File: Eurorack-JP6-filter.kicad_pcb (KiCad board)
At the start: 2 copper layers, 65 x 100 mm, 153 parts, among them J1 JACK_MONO_SW, J2 JACK_MONO_SW, J3 JACK_MONO_SW, J4 JACK_MONO_SW, J5 JACK_MONO_SW, J6 JACK_MONO_SW, P1 CONN_02X05, Q1 BCM857BS, Q2 BCM857BS, Q3 J112, Q4 J112, Q5 J112, Q6 J112, SW1 KS-01Q, U1 TL072-, U10 CD4027, U11 CD40106, U12 TS321, U13 TS321, U2 TL072-, U3 TL072-, U4 TL072-, U5 LM13700, U6 LM13700, U7 LM13700, U8 DG409, U9 CD4052

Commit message: cleaned up silkscreen a bit. ready to do panel alignment test
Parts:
- VR6: value 50K -> 50K A
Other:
- board text added: "CV 1 BI"
- board text added: "CV 2 UNI"
- board text added: "FREQ"
- board text added: "IN 1"
- board text added: "IN 2"
- board text added: "LEVEL 2"
- board text added: "M I M O I D"
- board text added: "MODE"
- board text added: "OUT"
- board text added: "RES"
- board text added: "RES CV"
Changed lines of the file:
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@@
     (area 11.949999 11.949999 77.050001 112.050001)
     (thickness 1.6)
-    (drawings 205)
-    (tracks 1138)
+    (drawings 216)
+    (tracks 1135)
     (zones 0)
     (modules 153)
@@
     (descr http://www.bourns.com/docs/Product-Datasheets/TC33.pdf)
     (tags "Bourns, trimmer")
-    (fp_text reference VR7 (at 0.85 -3.1) (layer B.SilkS)
+    (fp_text reference VR7 (at -2.85 1.6) (layer B.SilkS)
       (effects (font (size 0.8128 0.8128) (thickness 0.1524)) (justify mirror))
     )
@@
       (effects (font (thickness 0.3048)))
     )
-    (fp_text value 50K (at 0 9.99998 215) (layer F.SilkS)
+    (fp_text value "50K A" (at 0 9.99998 215) (layer F.SilkS)
       (effects (font (thickness 0.3048)))
     )
@@
   (module MyModules:PJ-301B-JACK-SLOTS (layer F.Cu)
     (at 19 106.5)
-    (fp_text reference J1 (at 4 -7) (layer F.SilkS)
+    (fp_text reference J1 (at 3.75 -4.75) (layer F.SilkS)
       (effects (font (size 1.5 1.5) (thickness 0.15)))
     )
@@
   (module MyModules:PJ-301B-JACK-SLOTS (layer F.Cu)
     (at 19 92.5)
-    (fp_text reference J2 (at 3.75 -7) (layer F.SilkS)
+    (fp_text reference J2 (at 3.5 -4.75) (layer F.SilkS)
       (effects (font (size 1.5 1.5) (thickness 0.15)))
     )
@@
   (module MyModules:PJ-301B-JACK-SLOTS (layer F.Cu)
     (at 70 92.5)
-    (fp_text reference J3 (at 4 -7) (layer F.SilkS)
+    (fp_text reference J3 (at 3.5 -4.75) (layer F.SilkS)
       (effects (font (size 1.5 1.5) (thickness 0.15)))
     )
@@
   (module MyModules:PJ-301B-JACK-SLOTS (layer F.Cu)
     (at 56 106.5)
-    (fp_text reference J4 (at 3.75 -7) (layer F.SilkS)
+    (fp_text reference J4 (at 3.5 -4.75) (layer F.SilkS)
       (effects (font (size 1.5 1.5) (thickness 0.15)))
     )
@@
   (module MyModules:PJ-301B-JACK-SLOTS (layer F.Cu)
     (at 33 106.5)
-    (fp_text reference J5 (at 4 -7) (layer F.SilkS)
+    (fp_text reference J5 (at 3.75 -4.75) (layer F.SilkS)
       (effects (font (size 1.5 1.5) (thickness 0.15)))
     )
@@
   (module MyModules:PJ-301B-JACK-SLOTS (layer F.Cu)
     (at 70 106.5)
-    (fp_text reference J6 (at 4 -7) (layer F.SilkS)
+    (fp_text reference J6 (at 3.5 -4.75) (layer F.SilkS)
       (effects (font (size 1.5 1.5) (thickness 0.15)))
     )
@@
     (at 33 81.5)
     (attr smd)
-    (fp_text reference R49 (at -2 0 90) (layer B.SilkS)
+    (fp_text reference R49 (at 0 -1.4 180) (layer B.SilkS)
       (effects (font (size 0.6096 0.6096) (thickness 0.1524)) (justify mirror))
     )
@@
       (xy 0.555814 2.531069)) (layer B.SilkS) (width 0.01))
   )
+  (gr_text MODE (at 54.75 15) (layer F.SilkS)
+    (effects (font (size 1.5 1.5) (thickness 0.3)))
+  )
+  (gr_text FREQ (at 37.25 15) (layer F.SilkS)
+    (effects (font (size 1.5 1.5) (thickness 0.3)))
+  )
+  (gr_text RES (at 30.75 56.5) (layer F.SilkS)
+    (effects (font (size 1.5 1.5) (thickness 0.3)))
+  )
+  (gr_text "LEVEL 2" (at 58.25 56.75) (layer F.SilkS)
+    (effects (font (size 1.5 1.5) (thickness 0.3)))
+  )
+  (gr_text OUT (at 70 99.25) (layer F.SilkS)
+    (effects (font (size 1.5 1.5) (thickness 0.3)))
+  )
+  (gr_text "IN 2" (at 56.25 99.25) (layer F.SilkS)
+    (effects (font (size 1.5 1.5) (thickness 0.3)))
+  )
+  (gr_text "IN 1" (at 33 99.5) (layer F.SilkS)
+    (effects (font (size 1.5 1.5) (thickness 0.3)))
+  )
+  (gr_text "RES CV" (at 19 99.25) (layer F.SilkS)
+    (effects (font (size 1.5 1.5) (thickness 0.3)))
+  )
+  (gr_text "CV 1\nBI" (at 23 84) (layer F.SilkS)
+    (effects (font (size 1.5 1.5) (thickness 0.3)))
+  )
+  (gr_text "CV 2\nUNI" (at 66.5 84) (layer F.SilkS)
+    (effects (font (size 1.5 1.5) (thickness 0.3)))
+  )
+  (gr_text "M I M O I D" (at 44.7 51.1) (layer F.SilkS)
+    (effects (font (size 1.5 1.5) (thickness 0.3)))
+  )
   (gr_line (start 65.343549 67.620649) (end 65.343549 67.620649) (layer B.SilkS) (width 0.35))
   (gr_line (start 65.343549 67.620649) (end 65.343549 67.620649) (layer B.SilkS) (width 0.35))
@@
     (effects (font (size 1.5 1.5) (thickness 0.3)) (justify mirror))
   )
-  (gr_text "Multimode Filter\nv1.3 10 2016\n" (at 67 83.25) (layer B.SilkS)
+  (gr_text "Multimode Filter\nv1.3 10 2016\n" (at 22.1 82.7) (layer B.SilkS)
     (effects (font (size 1.5 1.5) (thickness 0.3)) (justify mirror))
   )
-  (gr_text -12V (at 74.6 41.4) (layer B.SilkS)
+  (gr_text -12V (at 69.7 42.9 270) (layer B.SilkS)
     (effects (font (size 1.016 1.016) (thickness 0.254)) (justify mirror))
   )
-  (gr_text "RES\nADJ" (at 27.2 42.2) (layer B.SilkS)
+  (gr_text "RES\nADJ" (at 18.7 42) (layer B.SilkS)
     (effects (font (size 0.8128 0.8128) (thickness 0.1524)) (justify mirror))
   )
@@
   (segment (start 50.6491 79.5) (end 50.6491 82) (width 0.254) (layer B.Cu) (net 19))
   (segment (start 49.6 82) (end 50.6491 82) (width 0.254) (layer B.Cu) (net 19))
+  (segment (start 47.4 83.4) (end 57.3 83.4) (width 0.3556) (layer F.Cu) (net 20))
+  (segment (start 57.3 83.4) (end 59.3 81.4) (width 0.3556) (layer F.Cu) (net 20))
+  (segment (start 59.3 81.4) (end 59.3 77.1) (width 0.3556) (layer F.Cu) (net 20))
+  (segment (start 59.3 77.1) (end 58.131801 75.931801) (width 0.3556) (layer F.Cu) (net 20))
+  (segment (start 48.815759 43.035141) (end 46.057295 43.035141) (width 0.3556) (layer F.Cu) (net 20))
+  (segment (start 58.131801 75.931801) (end 58.131801 46.131801) (width 0.3556) (layer F.Cu) (net 20))
+  (segment (start 58.131801 46.131801) (end 55.035141 43.035141) (width 0.3556) (layer F.Cu) (net 20))
+  (segment (start 55.035141 43.035141) (end 48.815759 43.035141) (width 0.3556) (layer F.Cu) (net 20))
   (segment (start 40.899096 30.8991) (end 40.999996 31) (width 0.6096) (layer B.Cu) (net 20))
   (segment (start 39.25 30.8991) (end 40.899096 30.8991) (width 0.6096) (layer B.Cu) (net 20))
@@
   (segment (start 29.775685 36.474315) (end 21.918537 36.474315) (width 0.6096) (layer B.Cu) (net 20))
   (segment (start 35.3509 30.8991) (end 29.775685 36.474315) (width 0.6096) (layer B.Cu) (net 20))
-  (segment (start 54.8509 42.8509) (end 53.070597 42.8509) (width 0.3556) (layer F.Cu) (net 20))
-  (segment (start 58.131801 46.131801) (end 54.8509 42.8509) (width 0.3556) (layer F.Cu) (net 20))
   (segment (start 46.057295 43.035141) (end 46.057295 44.307295) (width 0.3556) (layer F.Cu) (net 20))
   (segment (start 46.057295 44.307295) (end 46.75 45) (width 0.3556) (layer F.Cu) (net 20))
@@
   (via (at 62.7 35.6) (size 1.27) (layers F.Cu B.Cu) (net 20))
   (via (at 46.057295 43.035141) (size 1.27) (drill 0.635) (layers F.Cu B.Cu) (net 20))
-  (segment (start 53.070597 42.8509) (end 49 42.8509) (width 0.3556) (layer F.Cu) (net 20))
-  (segment (start 48.815759 43.035141) (end 49 42.8509) (width 0.3556) (layer F.Cu) (net 20))
-  (segment (start 46.057295 43.035141) (end 48.815759 43.035141) (width 0.3556) (layer F.Cu) (net 20))
-  (segment (start 53.070597 42.8509) (end 53.099981 42.880284) (width 0.3556) (layer F.Cu) (net 20))
   (segment (start 45.162519 66.745691) (end 45.797518 66.110692) (width 0.3556) (layer F.Cu) (net 20))
   (segment (start 23.75 15) (end 27.8 15) (width 0.6096) (layer F.Cu) (net 20))
@@
   (segment (start 41.3 15) (end 46.601981 15) (width 0.6096) (layer F.Cu) (net 20))
   (segment (start 46.601981 15) (end 47.351981 14.25) (width 0.6096) (layer F.Cu) (net 20))
-  (segment (start 47.4 83.4) (end 57.3 83.4) (width 0.3556) (layer F.Cu) (net 20))
-  (segment (start 57.3 83.4) (end 59.3 81.4) (width 0.3556) (layer F.Cu) (net 20))
-  (segment (start 59.3 81.4) (end 59.3 77.1) (width 0.3556) (layer F.Cu) (net 20))
-  (segment (start 59.3 77.1) (end 58.131801 75.931801) (width 0.3556) (layer F.Cu) (net 20))
-  (segment (start 58.131801 75.931801) (end 58.131801 46.131801) (width 0.3556) (layer F.Cu) (net 20))
   (segment (start 40.255941 77.7) (end 40 77.7) (width 0.3556) (layer F.Cu) (net 20))
   (segment (start 36 81.7) (end 36 94.601975) (width 0.3556) (layer F.Cu) (net 20))

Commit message: Gerbers generated and checked
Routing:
- net GND: track 31.7 -> 34.5 mm, vias 15 -> 17
- net Net-(R2-Pad2): track 21.6 -> 20.6 mm
- net Net-(C3-Pad1): track 61.6 -> 62.3 mm

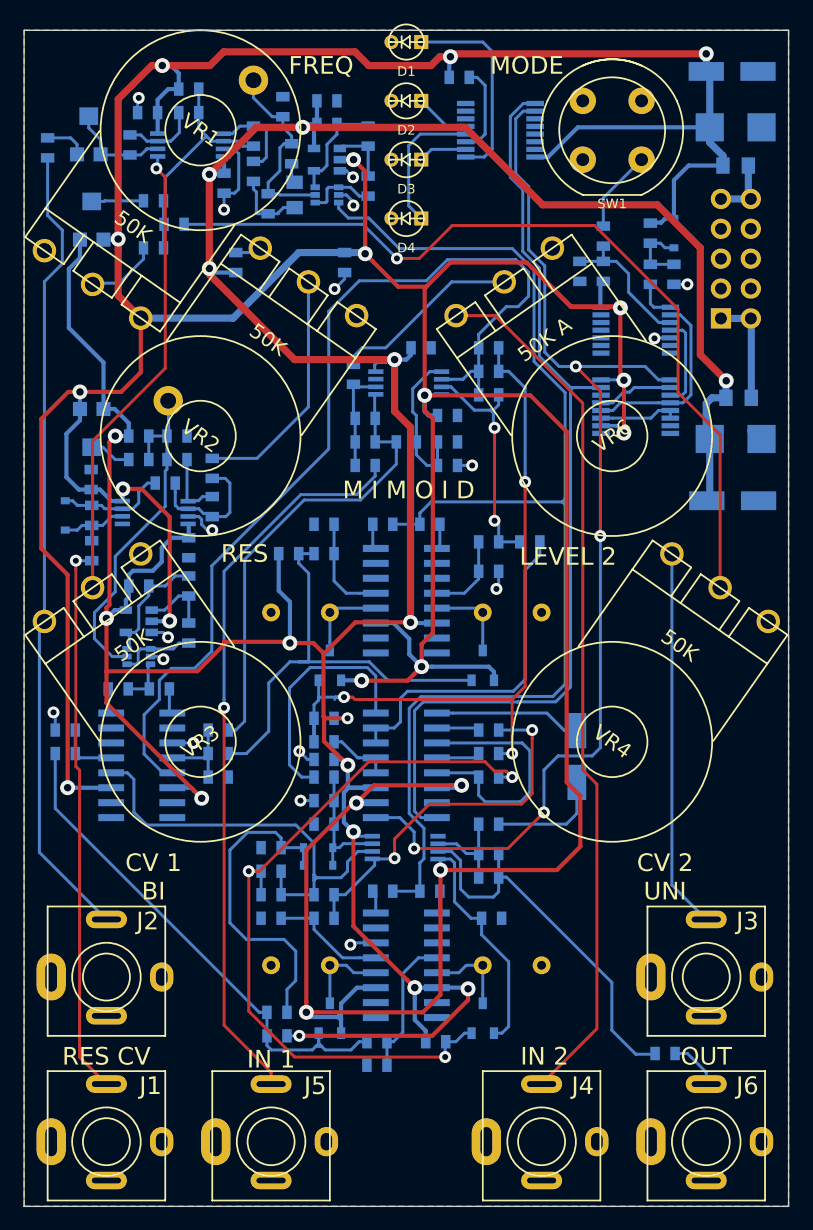
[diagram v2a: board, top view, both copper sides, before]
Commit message: fixed the cretinous error made by a cretin by which TS321 rails were reversed because said cretin can't pay attention to detail. Also added small pF caps in feedback of freq and res CV input stages
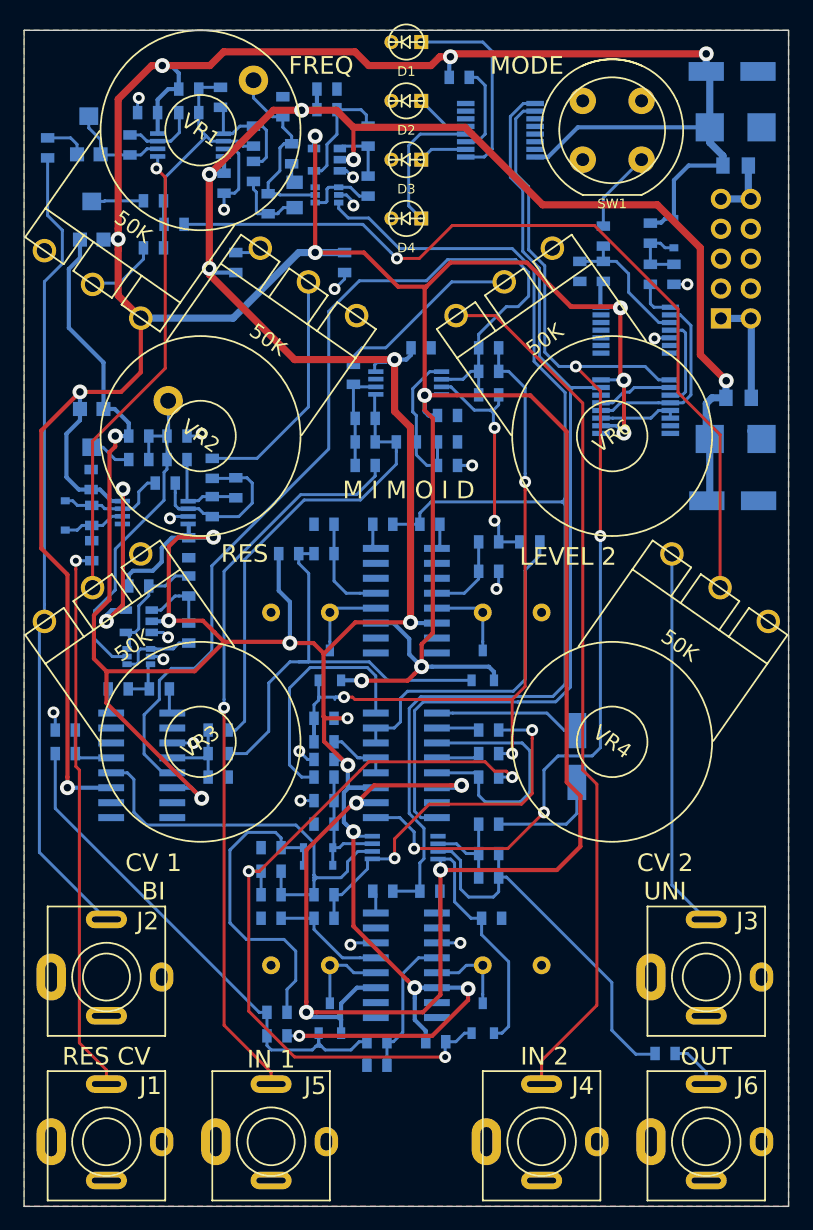
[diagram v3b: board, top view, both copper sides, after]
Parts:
- added C28: 22pF, MyModules:SM0603-C-JRL, B.Cu at (30.0, 50.9)
- added C29: 22pF, MyModules:SM0603-C-JRL, B.Cu at (28.7, 17.7)
- VR6: value 50K A -> 50K
- moved R28 1.25 mm to (37.8, 18.8)
- moved C15 1.00 mm to (37.8, 17.0)
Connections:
- U12 pad 2: +12V -> -12V
- U12 pad 5: -12V -> +12V
- U13 pad 2: +12V -> -12V
- U13 pad 5: -12V -> +12V
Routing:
- net -12V: track 318.1 -> 337.3 mm, vias 16 -> 18
- net Net-(C28-Pad2): track 11.2 -> 14.6 mm
- net Net-(C29-Pad1): track 7.61 -> 9.96 mm
- net Net-(C5-Pad2): track 9.29 -> 11.5 mm
- net +12V: track 491.6 -> 493.8 mm
- net GND: track 34.5 -> 36.7 mm, vias 17 -> 19
- net Net-(C28-Pad1): track 5.80 -> 7.85 mm
- net Net-(C29-Pad2): track 19.8 -> 21.7 mm

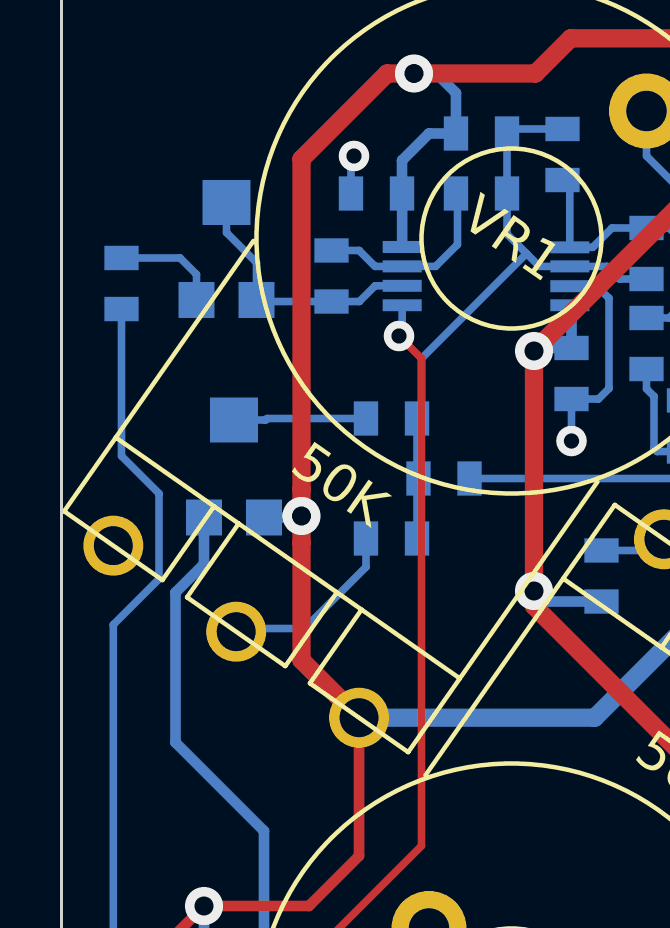
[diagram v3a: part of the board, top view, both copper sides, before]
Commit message: removed centre trimmer, doesn't seem to be required
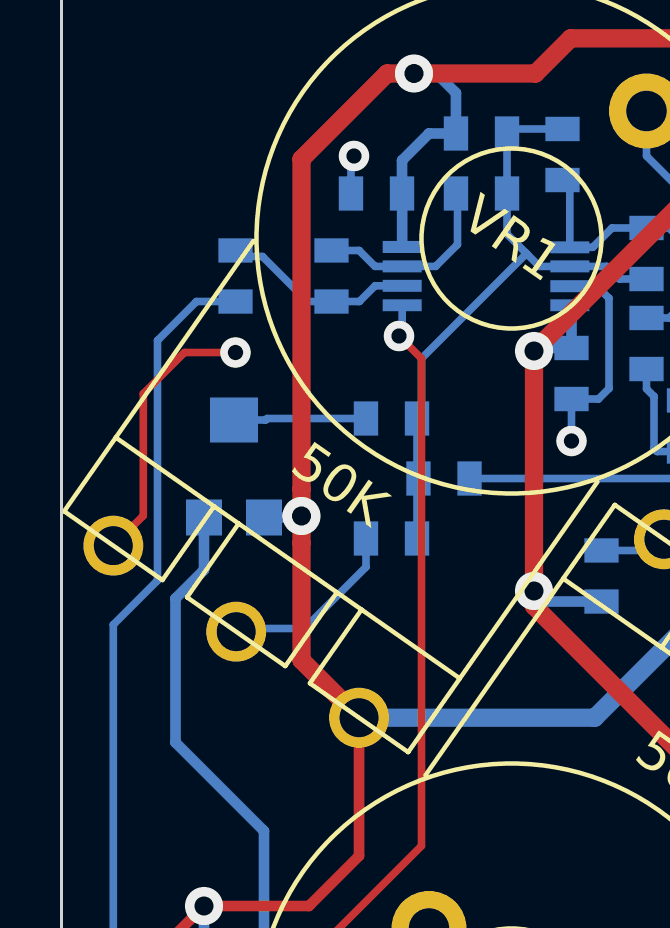
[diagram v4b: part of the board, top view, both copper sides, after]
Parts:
- removed REF***: OSHW-Symbol_6.7x6mm_SilkScreen, Symbols:OSHW-Symbol_6.7x6mm_SilkScreen
- removed VR8: 100K, MyModules:TC33X-2
- R41: value 10K -> 3.3K
- R76: value 47K -> 100K
- moved R76 3.81 mm to (17.8, 21.8)
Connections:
- R77 pad 2: Net-(R77-Pad2) -> Net-(R76-Pad1)
- U1 pad 6: Net-(R77-Pad2) -> Net-(R76-Pad1)
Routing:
- net GND: track 36.7 -> 45.8 mm, vias 19 -> 20
- net Net-(R77-Pad2): track 8.76 -> 0.00 mm
- net Net-(R76-Pad1): track 3.58 -> 6.48 mm
- net Net-(J2-Pad3): track 68.4 -> 70.0 mm
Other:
- board text removed: "CENTRE"

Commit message: generated BOM
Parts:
- J1, J2, J3, J4, J5, J6: value JACK_MONO_SW -> PJ301B
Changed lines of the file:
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@@
       (effects (font (size 1.5 1.5) (thickness 0.15)))
     )
-    (fp_text value JACK_MONO_SW (at 0 -8) (layer F.SilkS) hide
+    (fp_text value PJ301B (at 0 -8) (layer F.SilkS) hide
       (effects (font (size 1.5 1.5) (thickness 0.15)))
     )
@@
       (effects (font (size 1.5 1.5) (thickness 0.15)))
     )
-    (fp_text value JACK_MONO_SW (at 0 -8) (layer F.SilkS) hide
+    (fp_text value PJ301B (at 0 -8) (layer F.SilkS) hide
       (effects (font (size 1.5 1.5) (thickness 0.15)))
     )
@@
       (effects (font (size 1.5 1.5) (thickness 0.15)))
     )
-    (fp_text value JACK_MONO_SW (at 0 -8) (layer F.SilkS) hide
+    (fp_text value PJ301B (at 0 -8) (layer F.SilkS) hide
       (effects (font (size 1.5 1.5) (thickness 0.15)))
     )
@@
       (effects (font (size 1.5 1.5) (thickness 0.15)))
     )
-    (fp_text value JACK_MONO_SW (at 0 -8) (layer F.SilkS) hide
+    (fp_text value PJ301B (at 0 -8) (layer F.SilkS) hide
       (effects (font (size 1.5 1.5) (thickness 0.15)))
     )
@@
       (effects (font (size 1.5 1.5) (thickness 0.15)))
     )
-    (fp_text value JACK_MONO_SW (at 0 -8) (layer F.SilkS) hide
+    (fp_text value PJ301B (at 0 -8) (layer F.SilkS) hide
       (effects (font (size 1.5 1.5) (thickness 0.15)))
     )
@@
       (effects (font (size 1.5 1.5) (thickness 0.15)))
     )
-    (fp_text value JACK_MONO_SW (at 0 -8) (layer F.SilkS) hide
+    (fp_text value PJ301B (at 0 -8) (layer F.SilkS) hide
       (effects (font (size 1.5 1.5) (thickness 0.15)))
     )

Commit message: merge v1.3 into master, update readme
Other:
- board text added: "system80.net"
- board text removed: "system79.com"
